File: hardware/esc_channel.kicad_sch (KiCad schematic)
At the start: 17 parts, among them Q32 AGM210MAP, Q33 AGM210MAP, Q34 AGM210MAP, U7 EFM8BB51F16I

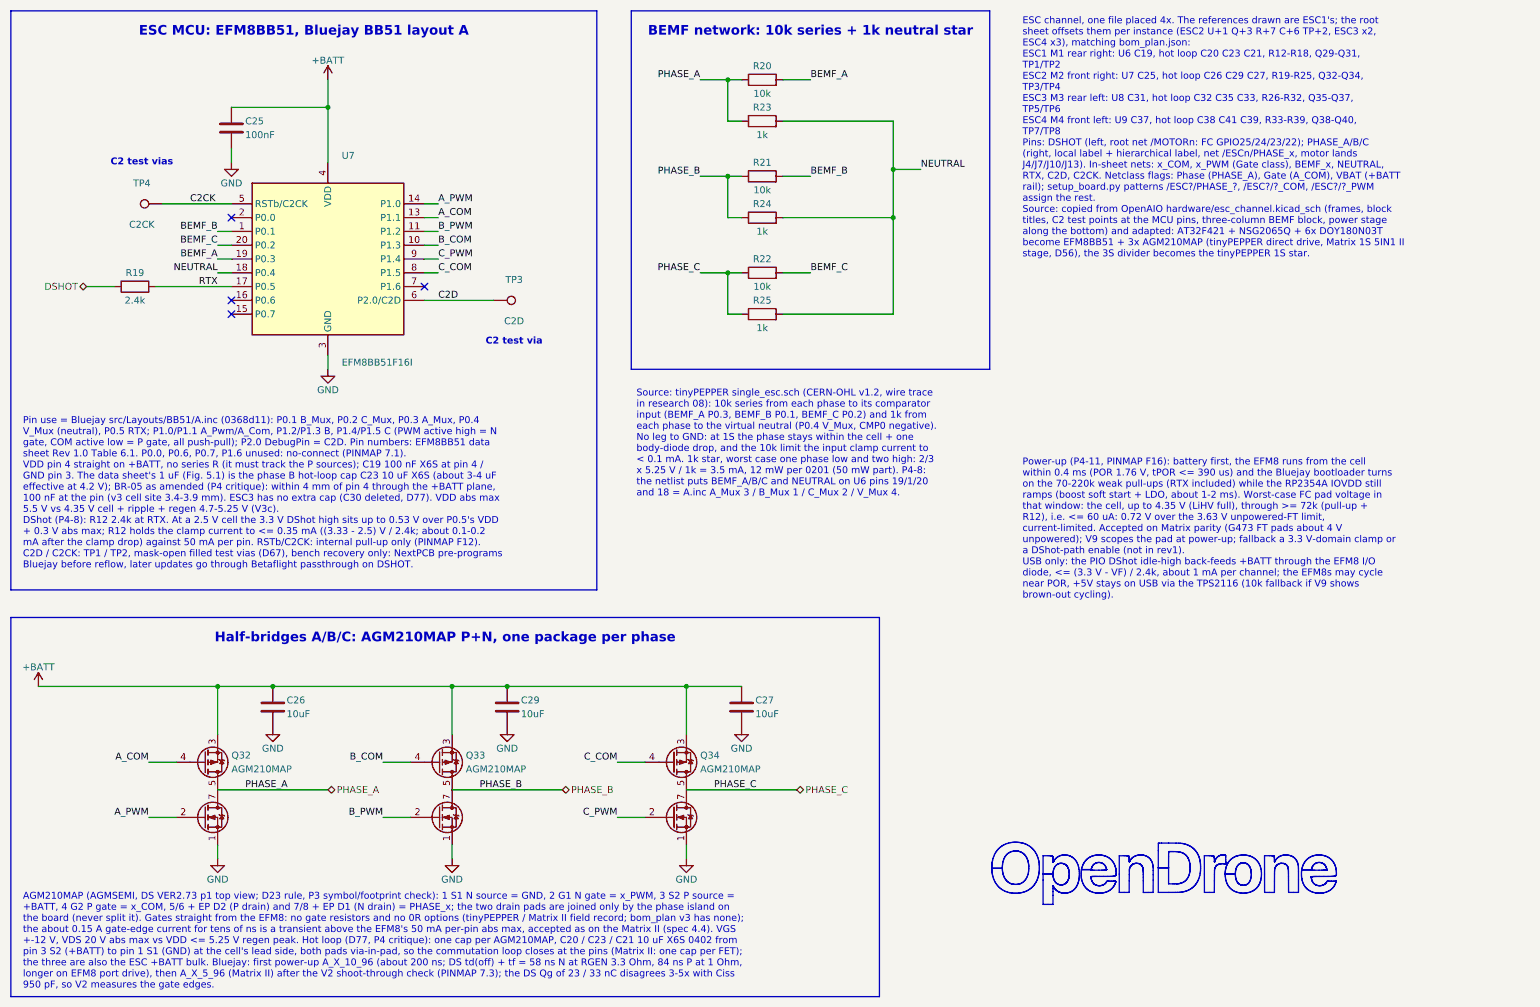
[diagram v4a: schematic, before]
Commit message: wip: routing prep (zones and via fields) and schematic review round 4
Co-Authored-By: Claude Opus 5.5 <noreply@anthropic.com>
Claude-Session: https://claude.ai/code/session_01RFaS5jnC9tnPam9GBgmGnG
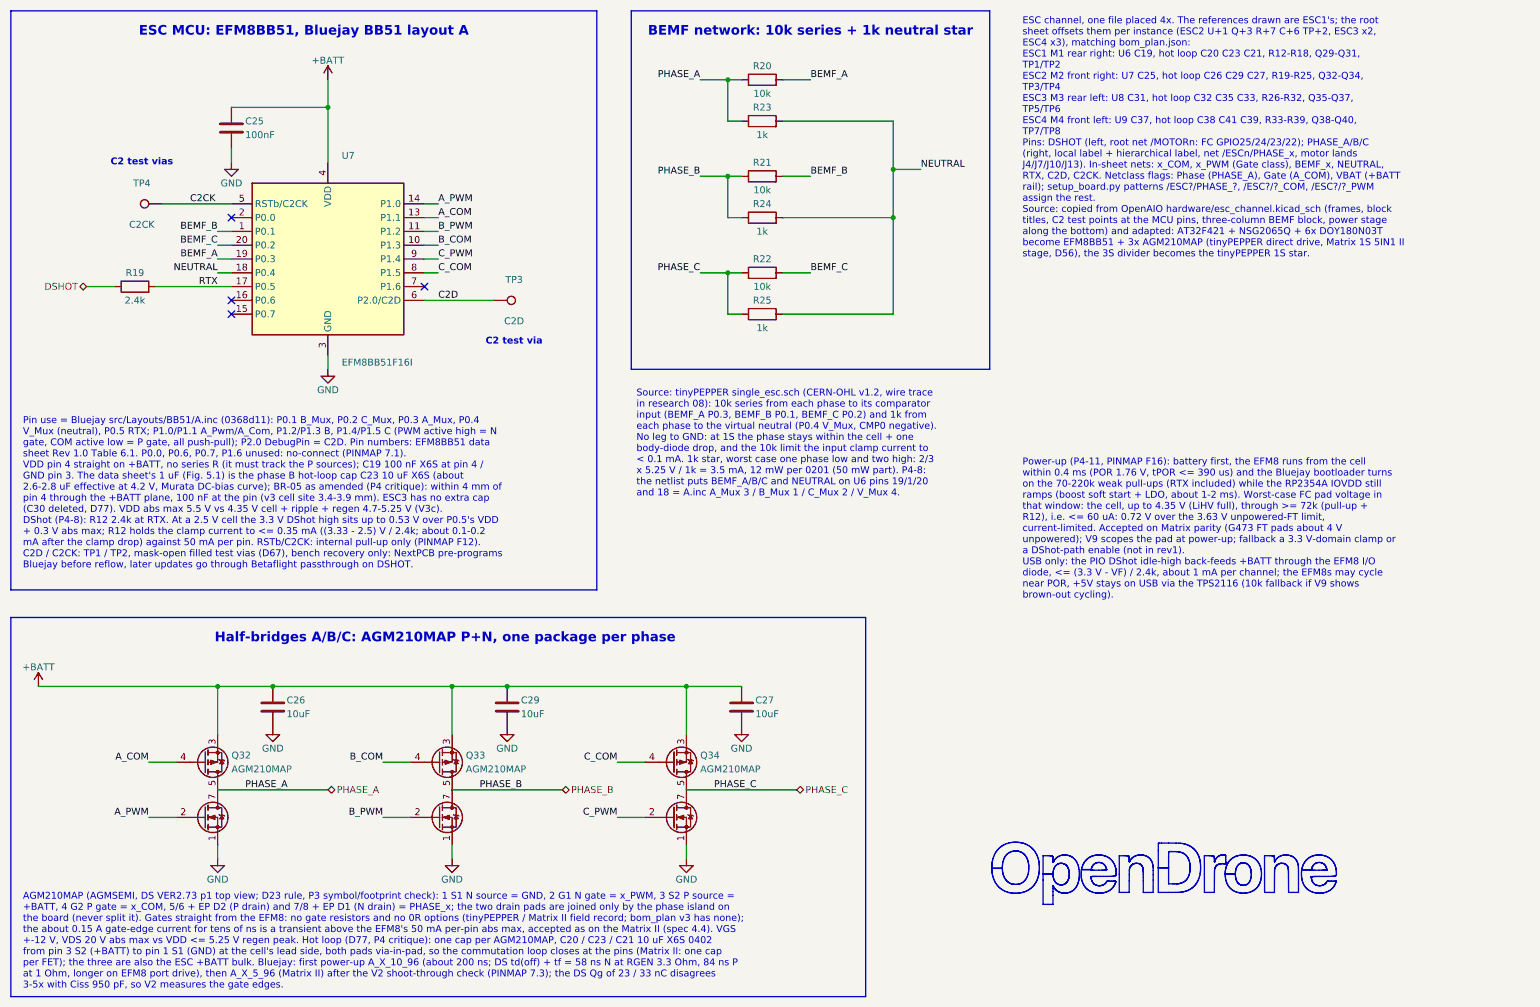
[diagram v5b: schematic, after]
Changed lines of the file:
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@@
 	(rectangle
 		(start 17.78 127)
-		(end 177.8 196.85)
+		(end 175.26 196.85)
 		(stroke
 			(width 0)
@@
 		(exclude_from_sim no)
 		(at 19.05 176.53 0)
-		(size 157.48 19.05)
+		(size 154.94 19.05)
 		(margins 0.9525 0.9525 0.9525 0.9525)
 		(stroke
@@
 		)
 	)
-	(text_box "Pin use = Bluejay src/Layouts/BB51/A.inc (0368d11): P0.1 B_Mux, P0.2 C_Mux, P0.3 A_Mux, P0.4 V_Mux (neutral), P0.5 RTX; P1.0/P1.1 A_Pwm/A_Com, P1.2/P1.3 B, P1.4/P1.5 C (PWM active high = N gate, COM active low = P gate, all push-pull); P2.0 DebugPin = C2D. Pin numbers: EFM8BB51 data sheet Rev 1.0 Table 6.1. P0.0, P0.6, P0.7, P1.6 unused: no-connect (PINMAP 7.1).\nVDD pin 4 straight on +BATT, no series R (it must track the P sources); C19 100 nF X6S at pin 4 / GND pin 3. The data sheet's 1 uF (Fig. 5.1) is the phase B hot-loop cap C23 10 uF X6S (about 3-4 uF effective at 4.2 V); BR-05 as amended (P4 critique): within 4 mm of pin 4 through the +BATT plane, 100 nF at the pin (v3 cell site 3.4-3.9 mm). ESC3 has no extra cap (C30 deleted, D77). VDD abs max 5.5 V vs 4.35 V cell + ripple + regen 4.7-5.25 V (V3c).\nDShot (P4-8): R12 2.4k at RTX. At a 2.5 V cell the 3.3 V DShot high sits up to 0.53 V over P0.5's VDD + 0.3 V abs max; R12 holds the clamp current to <= 0.35 mA ((3.33 - 2.5) V / 2.4k; about 0.1-0.2 mA after the clamp drop) against 50 mA per pin. RSTb/C2CK: internal pull-up only (PINMAP F12).\nC2D / C2CK: TP1 / TP2, mask-open filled test vias (D67), bench recovery only: NextPCB pre-programs Bluejay before reflow, later updates go through Betaflight passthrough on DSHOT."
+	(text_box "Pin use = Bluejay src/Layouts/BB51/A.inc (0368d11): P0.1 B_Mux, P0.2 C_Mux, P0.3 A_Mux, P0.4 V_Mux (neutral), P0.5 RTX; P1.0/P1.1 A_Pwm/A_Com, P1.2/P1.3 B, P1.4/P1.5 C (PWM active high = N gate, COM active low = P gate, all push-pull); P2.0 DebugPin = C2D. Pin numbers: EFM8BB51 data sheet Rev 1.0 Table 6.1. P0.0, P0.6, P0.7, P1.6 unused: no-connect (PINMAP 7.1).\nVDD pin 4 straight on +BATT, no series R (it must track the P sources); C19 100 nF X6S at pin 4 / GND pin 3. The data sheet's 1 uF (Fig. 5.1) is the phase B hot-loop cap C23 10 uF X6S (about 2.6-2.8 uF effective at 4.2 V, Murata DC-bias curve); BR-05 as amended (P4 critique): within 4 mm of pin 4 through the +BATT plane, 100 nF at the pin (v3 cell site 3.4-3.9 mm). ESC3 has no extra cap (C30 deleted, D77). VDD abs max 5.5 V vs 4.35 V cell + ripple + regen 4.7-5.25 V (V3c).\nDShot (P4-8): R12 2.4k at RTX. At a 2.5 V cell the 3.3 V DShot high sits up to 0.53 V over P0.5's VDD + 0.3 V abs max; R12 holds the clamp current to <= 0.35 mA ((3.33 - 2.5) V / 2.4k; about 0.1-0.2 mA after the clamp drop) against 50 mA per pin. RSTb/C2CK: internal pull-up only (PINMAP F12).\nC2D / C2CK: TP1 / TP2, mask-open filled test vias (D67), bench recovery only: NextPCB pre-programs Bluejay before reflow, later updates go through Betaflight passthrough on DSHOT."
 		(exclude_from_sim no)
 		(at 19.05 88.9 0)

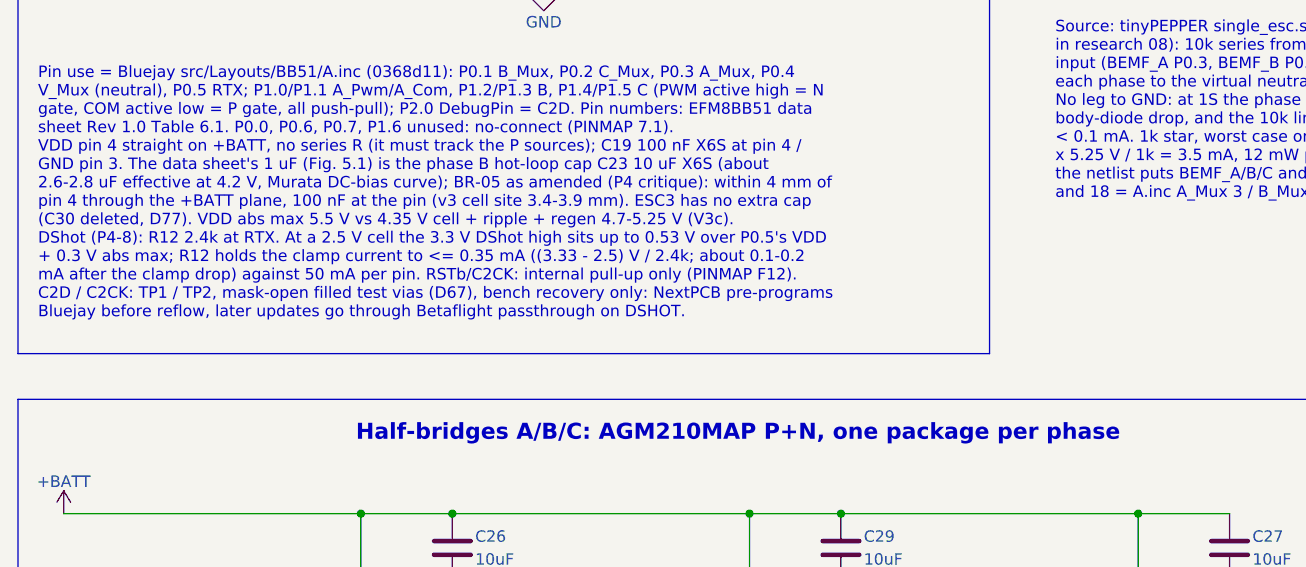
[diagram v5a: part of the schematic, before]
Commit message: schematic: review complete (4 rounds; U20 pin 1 to GND, footprint filters fixed, TPS22810DRVR, R54 270R); ERC 0 errors, check_netlist 7/7; D85-D87
Co-Authored-By: Claude Opus 5.5 <noreply@anthropic.com>
Claude-Session: https://claude.ai/code/session_01RFaS5jnC9tnPam9GBgmGnG
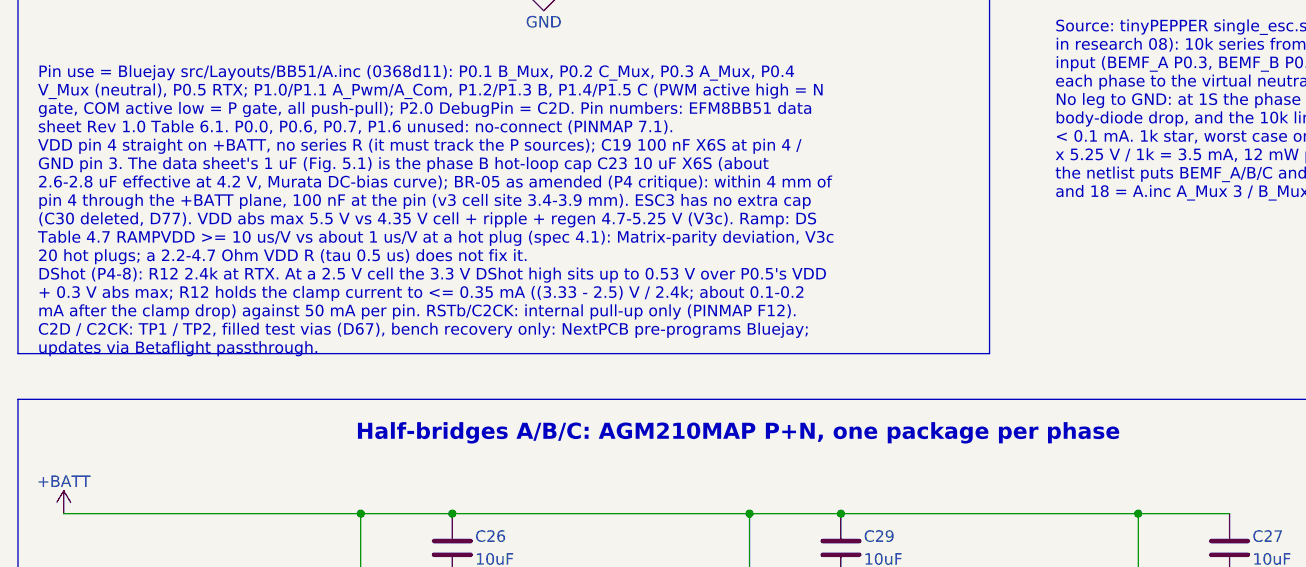
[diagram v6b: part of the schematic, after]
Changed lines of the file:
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@@
 		)
 	)
-	(text_box "Pin use = Bluejay src/Layouts/BB51/A.inc (0368d11): P0.1 B_Mux, P0.2 C_Mux, P0.3 A_Mux, P0.4 V_Mux (neutral), P0.5 RTX; P1.0/P1.1 A_Pwm/A_Com, P1.2/P1.3 B, P1.4/P1.5 C (PWM active high = N gate, COM active low = P gate, all push-pull); P2.0 DebugPin = C2D. Pin numbers: EFM8BB51 data sheet Rev 1.0 Table 6.1. P0.0, P0.6, P0.7, P1.6 unused: no-connect (PINMAP 7.1).\nVDD pin 4 straight on +BATT, no series R (it must track the P sources); C19 100 nF X6S at pin 4 / GND pin 3. The data sheet's 1 uF (Fig. 5.1) is the phase B hot-loop cap C23 10 uF X6S (about 2.6-2.8 uF effective at 4.2 V, Murata DC-bias curve); BR-05 as amended (P4 critique): within 4 mm of pin 4 through the +BATT plane, 100 nF at the pin (v3 cell site 3.4-3.9 mm). ESC3 has no extra cap (C30 deleted, D77). VDD abs max 5.5 V vs 4.35 V cell + ripple + regen 4.7-5.25 V (V3c).\nDShot (P4-8): R12 2.4k at RTX. At a 2.5 V cell the 3.3 V DShot high sits up to 0.53 V over P0.5's VDD + 0.3 V abs max; R12 holds the clamp current to <= 0.35 mA ((3.33 - 2.5) V / 2.4k; about 0.1-0.2 mA after the clamp drop) against 50 mA per pin. RSTb/C2CK: internal pull-up only (PINMAP F12).\nC2D / C2CK: TP1 / TP2, mask-open filled test vias (D67), bench recovery only: NextPCB pre-programs Bluejay before reflow, later updates go through Betaflight passthrough on DSHOT."
+	(text_box "Pin use = Bluejay src/Layouts/BB51/A.inc (0368d11): P0.1 B_Mux, P0.2 C_Mux, P0.3 A_Mux, P0.4 V_Mux (neutral), P0.5 RTX; P1.0/P1.1 A_Pwm/A_Com, P1.2/P1.3 B, P1.4/P1.5 C (PWM active high = N gate, COM active low = P gate, all push-pull); P2.0 DebugPin = C2D. Pin numbers: EFM8BB51 data sheet Rev 1.0 Table 6.1. P0.0, P0.6, P0.7, P1.6 unused: no-connect (PINMAP 7.1).\nVDD pin 4 straight on +BATT, no series R (it must track the P sources); C19 100 nF X6S at pin 4 / GND pin 3. The data sheet's 1 uF (Fig. 5.1) is the phase B hot-loop cap C23 10 uF X6S (about 2.6-2.8 uF effective at 4.2 V, Murata DC-bias curve); BR-05 as amended (P4 critique): within 4 mm of pin 4 through the +BATT plane, 100 nF at the pin (v3 cell site 3.4-3.9 mm). ESC3 has no extra cap (C30 deleted, D77). VDD abs max 5.5 V vs 4.35 V cell + ripple + regen 4.7-5.25 V (V3c). Ramp: DS Table 4.7 RAMPVDD >= 10 us/V vs about 1 us/V at a hot plug (spec 4.1): Matrix-parity deviation, V3c 20 hot plugs; a 2.2-4.7 Ohm VDD R (tau 0.5 us) does not fix it.\nDShot (P4-8): R12 2.4k at RTX. At a 2.5 V cell the 3.3 V DShot high sits up to 0.53 V over P0.5's VDD + 0.3 V abs max; R12 holds the clamp current to <= 0.35 mA ((3.33 - 2.5) V / 2.4k; about 0.1-0.2 mA after the clamp drop) against 50 mA per pin. RSTb/C2CK: internal pull-up only (PINMAP F12).\nC2D / C2CK: TP1 / TP2, filled test vias (D67), bench recovery only: NextPCB pre-programs Bluejay; updates via Betaflight passthrough."
 		(exclude_from_sim no)
 		(at 19.05 88.9 0)
